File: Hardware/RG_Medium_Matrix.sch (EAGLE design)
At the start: 24 parts, among them IC1 74LS595D, IC2 74LS595D, U2 AVR_SPI_PRG_6PTH, U3 16MHz

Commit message: Updating to locking footprints for SPI connectors
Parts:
- JP3: device SparkFun:M06SMD -> SparkFun-Connectors:M06LOCK
- JP4: device SparkFun:M06SIP -> SparkFun-Connectors:M06LOCK
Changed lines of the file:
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@@
 <part name="P+13" library="supply1" deviceset="VCC" device=""/>
 <part name="P+14" library="supply1" deviceset="VCC" device=""/>
-<part name="JP3" library="SparkFun" deviceset="M06" device="SMD"/>
-<part name="JP4" library="SparkFun" deviceset="M06" device="SIP"/>
+<part name="JP3" library="SparkFun-Connectors" deviceset="M06" device="LOCK"/>
+<part name="JP4" library="SparkFun-Connectors" deviceset="M06" device="LOCK"/>
 <part name="U3" library="SparkFun" deviceset="RESONATOR" device="SMD" value="16MHz"/>
 <part name="LOGO1" library="SparkFun-Aesthetics" deviceset="OSHW-LOGO" device="S" value="OSHW-LOGOS"/>

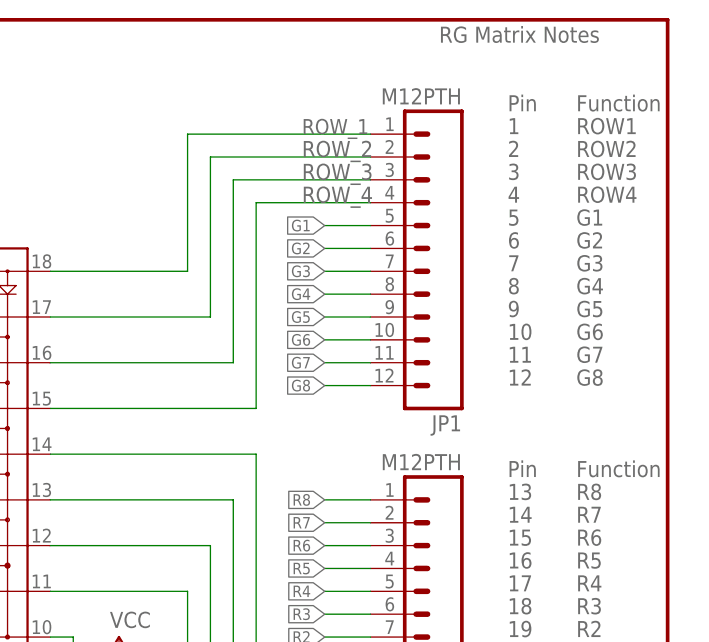
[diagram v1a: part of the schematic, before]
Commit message: Switching to locking fp for 12 pin headers
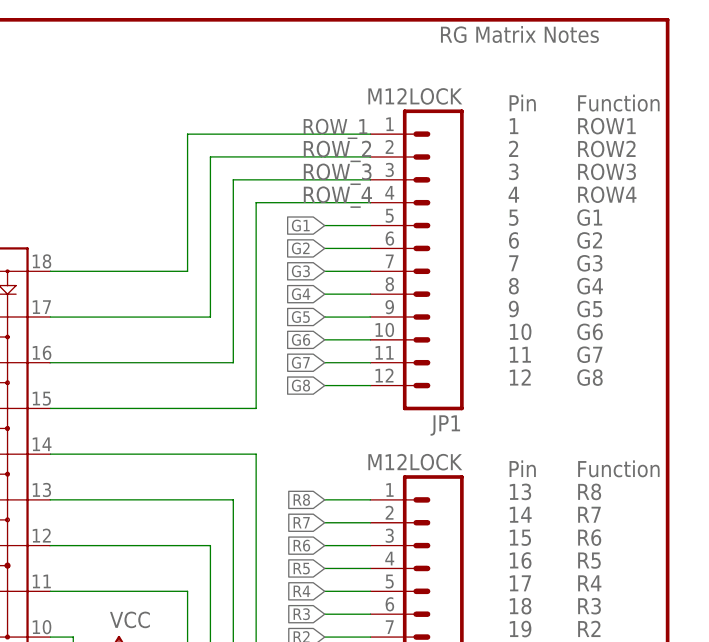
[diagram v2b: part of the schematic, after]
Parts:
- JP1, JP2: value M12PTH -> M12LOCK; device SparkFun:M12PTH -> SparkFun-Connectors:M12LOCK
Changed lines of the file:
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@@
 <part name="GND10" library="SparkFun" deviceset="GND" device=""/>
 <part name="GND11" library="SparkFun" deviceset="GND" device=""/>
-<part name="JP1" library="SparkFun" deviceset="M12" device="PTH"/>
-<part name="JP2" library="SparkFun" deviceset="M12" device="PTH"/>
+<part name="JP1" library="SparkFun-Connectors" deviceset="M12" device="LOCK"/>
+<part name="JP2" library="SparkFun-Connectors" deviceset="M12" device="LOCK"/>
 <part name="P+11" library="supply1" deviceset="VCC" device=""/>
 <part name="GND14" library="SparkFun" deviceset="GND" device=""/>
